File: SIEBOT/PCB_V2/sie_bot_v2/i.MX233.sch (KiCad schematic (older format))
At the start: 88 parts, among them IC1 iMX233, J1 MICROSD, J2 POWER_5V, P1 CONN_12X2, P10 CONN_1, P2 CONN_12X2, P3 CONN_1, P4 CONN_4X2, P5 CONN_1, P6 CONN_2, P7 CONN_1, Q1 MMDT3904, SW3 RESET, U1 ADM3101E, X1 24MHz

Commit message: Adición de ejemplos, modificación de los fuentes de elua para soportar el stm32f105
Cambios en el PCB para tener comunicación entre el IMX y el STM32 por puerto serial e i2c
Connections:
- net labels added: AUART_RX, AUART_TX
- net labels removed: SSPI_DATA1, SSPI_DATA2
- wire segments 394 -> 392
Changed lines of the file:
@@
-EESchema Schematic File Version 2  date Sat 21 Jan 2012 09:46:46 PM COT
+EESchema Schematic File Version 2  date Fri 10 Feb 2012 10:54:05 AM COT
 LIBS:con-jack
 LIBS:adm3101e
@@
 $Descr A3 16535 11700
 encoding utf-8
-Sheet 3 5
+Sheet 2 5
 Title ""
-Date "22 jan 2012"
+Date "10 feb 2012"
 Rev ""
 Comp ""
@@
 Comment4 ""
 $EndDescr
+Text HLabel 1950 6800 0    60   BiDi ~ 0
+AUART_TX
+Text HLabel 1950 6700 0    60   BiDi ~ 0
+AUART_RX
 Text Label 13050 5000 0    60   ~ 0
 GND
@@
 	11800 9000 12500 9000
 Wire Wire Line
-	11800 9200 12500 9200
-Wire Wire Line
 	12850 5000 13600 5000
 Wire Wire Line
@@
 Wire Wire Line
 	12500 9100 11800 9100
-Wire Wire Line
-	12500 9300 11800 9300
 Wire Wire Line
 	15150 5000 14400 5000
@@
 Text HLabel 12500 9100 2    60   BiDi ~ 0
 GPMI_CE0N
-Text HLabel 12500 9200 2    60   BiDi ~ 0
-SSPI_DATA1
 Text HLabel 12500 9550 2    60   BiDi ~ 0
 SSPI_DETECT
-Text HLabel 12500 9300 2    60   BiDi ~ 0
-SSPI_DATA2
 Text HLabel 12500 9000 2    60   BiDi ~ 0
 GPMI_CE1N
@@
 Text Label 13550 4900 2    60   ~ 0
 SSPI_DATA3
-Text Label 12300 9200 2    60   ~ 0
-SSPI_DATA1
-Text Label 12300 9300 2    60   ~ 0
-SSPI_DATA2
 Text Label 13450 4800 2    60   ~ 0
 SSPI_CMD
@@
 Text Label 2450 7100 2    60   ~ 0
 SSPI_DATA0
-Text Label 2450 7200 2    60   ~ 0
-SSPI_DATA1
-Text Label 2450 7300 2    60   ~ 0
-SSPI_DATA2
 Text Label 2300 7600 2    60   ~ 0
 SSPI_SCK
@@
 Text Label 11800 9700 0    60   ~ 0
 I2C_SDA
-Text Label 2050 6800 0    60   ~ 0
+Text Label 1950 7200 0    60   ~ 0
 I2C_SCL
-Text Label 2050 6700 0    60   ~ 0
+Text Label 1950 7300 0    60   ~ 0
 I2C_SDA
 Text Label 6250 6950 0    60   ~ 0

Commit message: Se elimina J2 (jack power) y el pulsador de reset y se dejan estas señales disponibles en los conectores, esto se hace para que esta board se adapte fácil a diferentes plataformas Se cambian las señales TDi y TDO que van del IMX al JTAG del stm32 por PWM2 y GPMI_CE1N, para dejar las señales del I2C del IMX disponibles.
Se conectan las señales SCL (pin 95) y SDA (pin 86) del iMX al bus I2C del STM32.

Se conectan resistencias de pull-up al bus I2C entre el IMX y el STM32

Se coloca una resistencia en serie a la salida de la señal TDO del STM32, esto para evitar que daños cuando los dos chips configuren esta señal como salida.

Se eliminan los conectores individuales de los motores y se organizan en un nuevo conector. Ahora los puentes H tienen el mismo voltaje de alimentación.

Se elimina la conexión entre BOOT0 y el IMX, ya que no es necesario modificar la forma de inicialización. Se elimina la resistencia de pull-up que se conecta a BOOT1.
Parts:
- removed J2: POWER_5V, symbol CONN_3
- removed P6: CONN_2, symbol CONN_2
- removed SW3: RESET, PB2, symbol RESET
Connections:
- net labels added: RESET_PB
- wire segments 392 -> 378
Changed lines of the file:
@@
-EESchema Schematic File Version 2  date Fri 10 Feb 2012 10:54:05 AM COT
+EESchema Schematic File Version 2  date Fri 10 Feb 2012 05:02:18 PM COT
 LIBS:con-jack
 LIBS:adm3101e
@@
 Comment4 ""
 $EndDescr
-Text HLabel 1950 6800 0    60   BiDi ~ 0
-AUART_TX
-Text HLabel 1950 6700 0    60   BiDi ~ 0
-AUART_RX
-Text Label 13050 5000 0    60   ~ 0
-GND
+Text Label 14450 4050 0    60   ~ 0
+RESET_PB
+Text Label 9250 2800 0    60   ~ 0
+RESET_PB
+Wire Wire Line
+	9150 2800 9700 2800
+Wire Wire Line
+	10000 4750 9500 4750
 Connection ~ 11050 6900
 Wire Wire Line
@@
 	14350 4150 14850 4150
 Wire Wire Line
-	14950 4150 14950 4050
-Wire Wire Line
-	14950 4050 14350 4050
-Wire Wire Line
 	15300 4850 15300 4800
 Wire Wire Line
@@
 Wire Wire Line
 	4850 10550 3500 10550
-Wire Wire Line
-	9500 2950 9500 3050
-Wire Wire Line
-	9200 3100 9200 3050
 Wire Notes Line
 	12000 550  10050 550
@@
 	1150 1850 1200 1850
 Wire Wire Line
-	11050 5300 11150 5300
-Wire Wire Line
-	11200 5350 11150 5350
-Wire Wire Line
 	4000 8250 4600 8250
 Wire Wire Line
@@
 Wire Wire Line
 	13300 700  12850 700
-Wire Wire Line
-	9500 4900 9500 4850
-Wire Wire Line
-	9500 4850 9800 4850
 Wire Wire Line
 	8550 6800 8550 6750
@@
 Wire Wire Line
 	10800 2900 10800 2800
-Wire Wire Line
-	9700 2800 9500 2800
 Wire Wire Line
 	10450 2850 10450 2800
@@
 Connection ~ 10450 2800
 Wire Wire Line
-	8550 2800 8900 2800
-Wire Wire Line
 	2550 6800 1950 6800
 Wire Notes Line
@@
 Connection ~ 4050 1600
 Wire Wire Line
-	9800 4850 9800 4900
-Wire Wire Line
 	9000 6900 9350 6900
 Wire Wire Line
@@
 Wire Wire Line
 	13350 7250 12950 7250
-Connection ~ 9800 4750
 Wire Wire Line
 	6750 1650 6750 1500
@@
 	12550 500  16000 500
 Wire Wire Line
-	10000 4750 9500 4750
-Wire Wire Line
 	9500 4750 9500 4700
 Wire Wire Line
@@
 Wire Wire Line
 	6600 8100 6650 8100
-Wire Wire Line
-	11150 5500 11050 5500
-Wire Wire Line
-	11050 5400 11150 5400
-Wire Wire Line
-	11150 5400 11150 5300
-Connection ~ 11150 5350
 Connection ~ 1150 1800
 Connection ~ 1100 1800
@@
 Wire Wire Line
 	11425 1200 11525 1200
-Wire Wire Line
-	8900 2950 8900 3050
-Wire Wire Line
-	8900 3050 9500 3050
-Connection ~ 9200 3050
 Connection ~ 2400 9300
 Connection ~ 2400 9700
@@
 	10450 6850 11050 6850
 Connection ~ 11050 6850
+Wire Wire Line
+	15050 4050 14350 4050
+Text HLabel 1900 6500 0    60   BiDi ~ 0
+PWM2
+Text HLabel 1950 6800 0    60   BiDi ~ 0
+AUART_TX
+Text HLabel 1950 6700 0    60   BiDi ~ 0
+AUART_RX
+Text Label 13050 5000 0    60   ~ 0
+GND
 $Comp
 L VDD5V #PWR91
@@
 $EndComp
 $Comp
-L VDD5V #PWR59
-U 1 1 4E78F92C
-P 8550 2800
-F 0 "#PWR59" H 8550 2900 30  0001 C CNN
-F 1 "VDD5V" H 8550 2900 30  0000 C CNN
-	1    8550 2800
-	1    0    0    -1
-$EndComp
-$Comp
 L GND #PWR97
 U 1 1 4E4D03B1
@@
 F 1 "GND" H 11550 1280 30  0001 C CNN
 	1    11550 1350
-	1    0    0    -1
-$EndComp
-$Comp
-L GND #PWR64
-U 1 1 4E455CD6
-P 9200 3100
-F 0 "#PWR64" H 9200 3100 30  0001 C CNN
-F 1 "GND" H 9200 3030 30  0001 C CNN
-	1    9200 3100
-	1    0    0    -1
-$EndComp
-$Comp
-L RESET SW3
-U 1 1 4E455CB6
-P 9200 2800
-F 0 "SW3" H 9350 2910 50  0000 C CNN
-F 1 "RESET" H 9200 2720 50  0000 C CNN
-F 2 "PB2" H 9200 2800 60  0001 C CNN
-	1    9200 2800
 	1    0    0    -1
 $EndComp
@@
 	1    1600 1800
 	0    1    1    0
-$EndComp
-$Comp
-L CONN_3 J2
-U 1 1 4E41CC3C
-P 10700 5400
-F 0 "J2" V 10650 5400 50  0000 C CNN
-F 1 "POWER_5V" V 10750 5400 40  0000 C CNN
-	1    10700 5400
-	-1   0    0    1
 $EndComp
 $Comp
@@
 	1    0    0    -1
 $EndComp
-$Comp
-L GND #PWR80
-U 1 1 4DA877BD
-P 11200 5350
-F 0 "#PWR80" H 11200 5350 30  0001 C CNN
-F 1 "GND" H 11200 5280 30  0001 C CNN
-	1    11200 5350
-	0    -1   -1   0
-$EndComp
-$Comp
-L VDD5V #PWR79
-U 1 1 4DA877B4
-P 11150 5500
-F 0 "#PWR79" H 11150 5600 30  0001 C CNN
-F 1 "VDD5V" H 11150 5600 30  0000 C CNN
-	1    11150 5500
-	0    1    1    0
-$EndComp
-$Comp
-L CONN_2 P6
-U 1 1 4DA86970
-P 9150 4800
-F 0 "P6" V 9100 4800 40  0000 C CNN
-F 1 "CONN_2" V 9200 4800 40  0000 C CNN
-	1    9150 4800
-	-1   0    0    -1
-$EndComp
 Text Label 9000 6950 0    45   ~ 0
 D03
@@
 Text Label 14450 4150 0    60   ~ 0
 TX
-$Comp
-L GND #PWR103
-U 1 1 4D7E9F5A
-P 14950 4150
-F 0 "#PWR103" H 14950 4150 30  0001 C CNN
-F 1 "GND" H 14950 4080 30  0001 C CNN
-	1    14950 4150
-	1    0    0    -1
-$EndComp
 $Comp
 L GND #PWR88
@@
 L VDD5V #PWR70
 U 1 1 4D4AB9B5
-P 9800 4750
-F 0 "#PWR70" H 9800 4850 30  0001 C CNN
-F 1 "VDD5V" H 9800 4850 30  0000 C CNN
-	1    9800 4750
-	1    0    0    -1
-$EndComp
-$Comp
-L GND #PWR71
-U 1 1 4D4AB9A9
-P 9800 4900
-F 0 "#PWR71" H 9800 4900 30  0001 C CNN
-F 1 "GND" H 9800 4830 30  0001 C CNN
-	1    9800 4900
+P 9500 4700
+F 0 "#PWR70" H 9500 4800 30  0001 C CNN
+F 1 "VDD5V" H 9500 4800 30  0000 C CNN
+	1    9500 4700
 	1    0    0    -1
 $EndComp
@@
 Text Label 1900 2300 0    60   ~ 0
 PSWITCH
-Text Label 13000 5100 0    60   ~ 0
-PWM2
 Text Label 1900 6300 0    60   ~ 0
 PWM0
 Text Label 1900 6400 0    60   ~ 0
 PWM1
-Text Label 1900 6500 0    60   ~ 0
-PWM2
 Text Label 6250 7500 0    60   ~ 0
 VAG

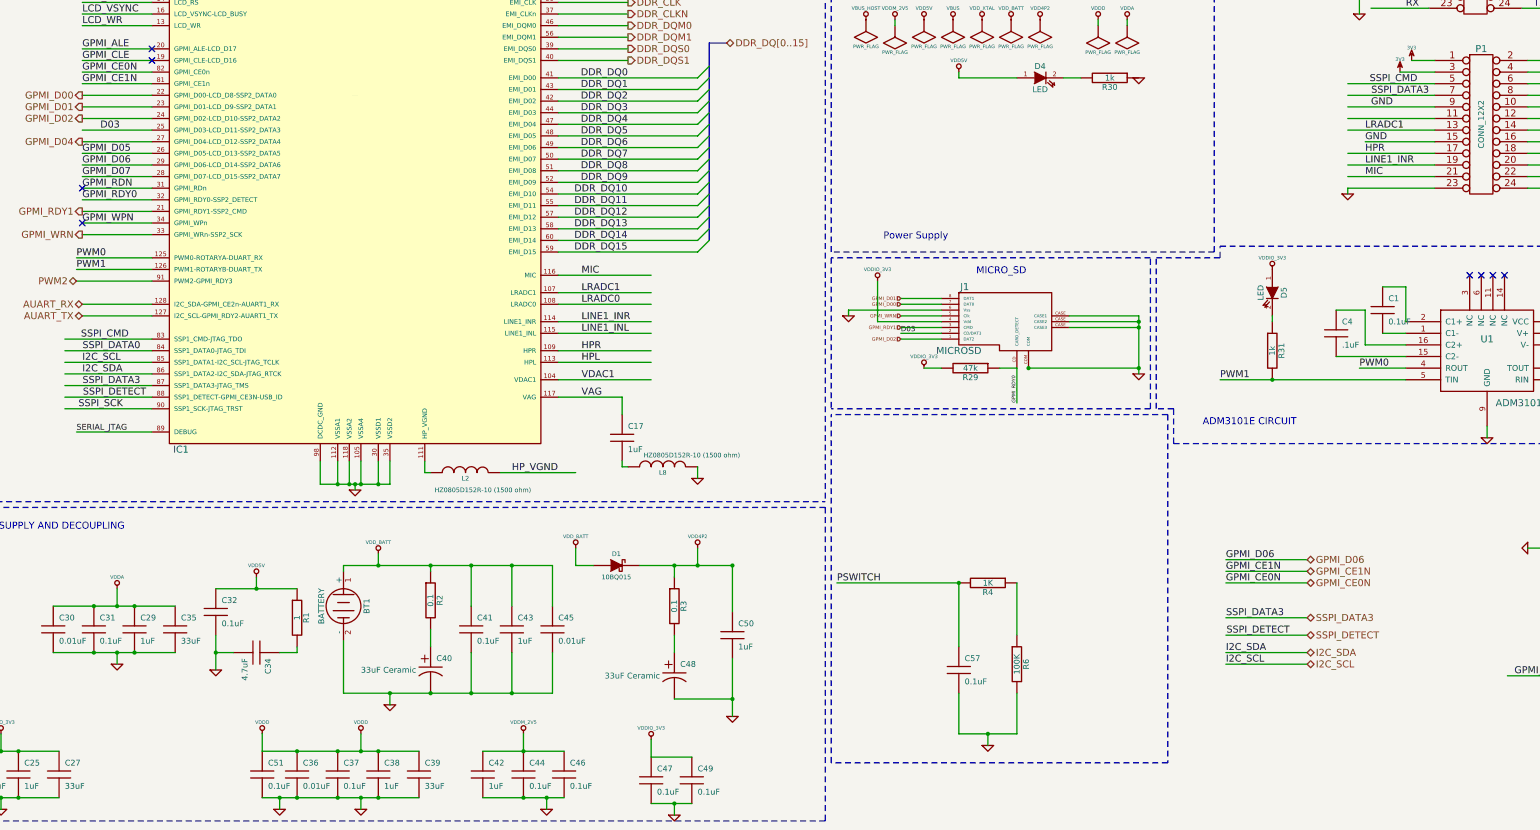
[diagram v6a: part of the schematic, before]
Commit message: Adición de r48 y r49 para llevar DO3 chip_select a la sd o a la memoria SPI
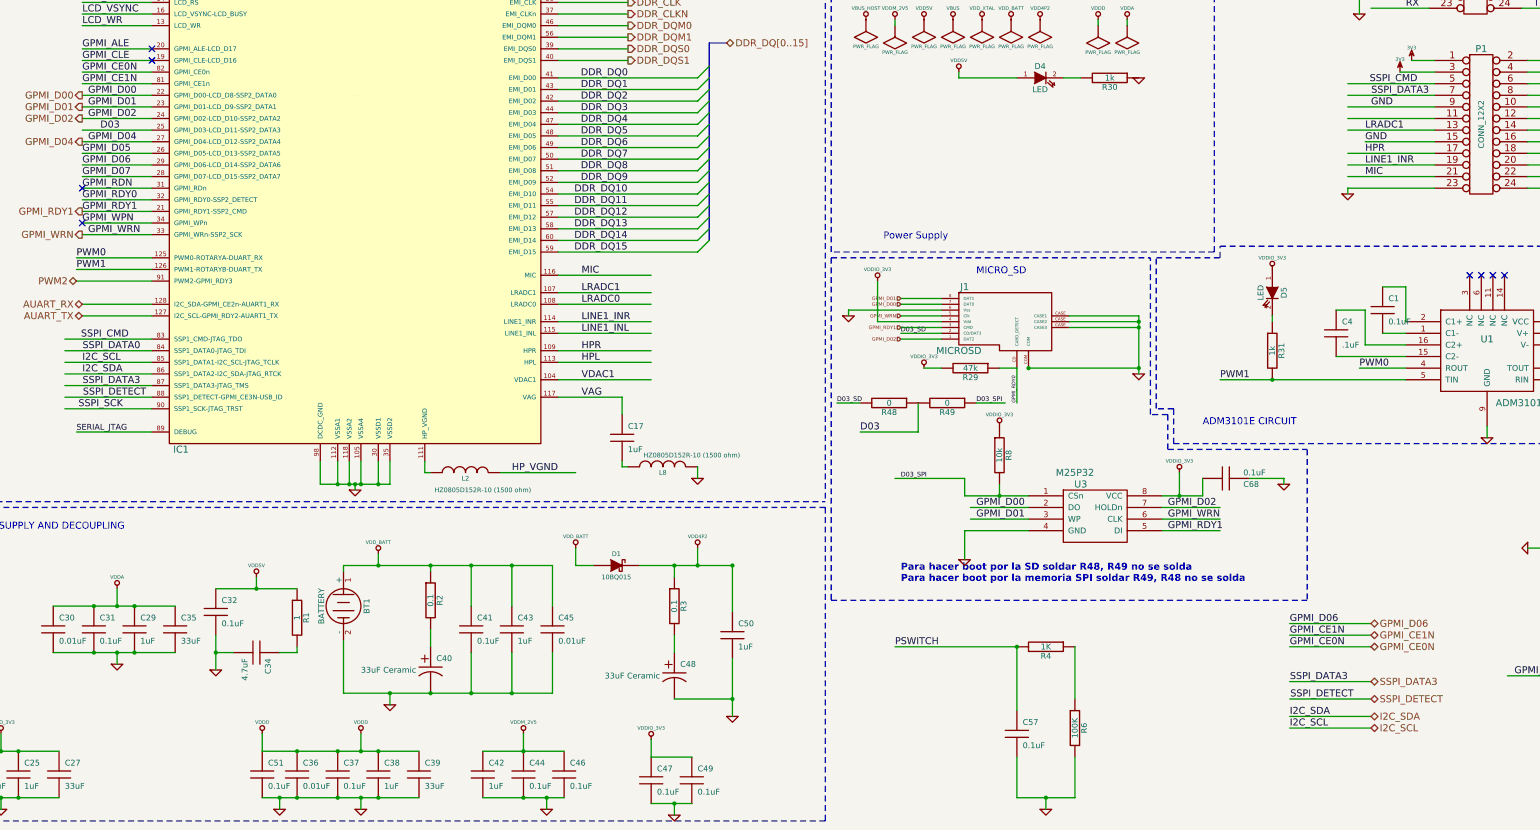
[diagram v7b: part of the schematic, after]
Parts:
- added C68: 0.1uF, symbol C
- added R48, R49: 0, sm0805, symbol R
- added R8: 10k, symbol R
- added U3: M25P32, SO16W, symbol M25P32
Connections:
- net labels added: D03_SD, D03_SPI
- wire segments 378 -> 398
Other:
- note added: "Para hacer boot por la SD soldar R48, R49 no se solda\nPara hacer boot por la memoria SPI soldar R49, R48 no se solda\n"
- moved on the sheet: C57, R4, R6
